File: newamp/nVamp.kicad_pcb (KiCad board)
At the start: 2 copper layers, 8 parts, among them J1 CONN_01X02, J2 CONN_01X02, U1 TS912

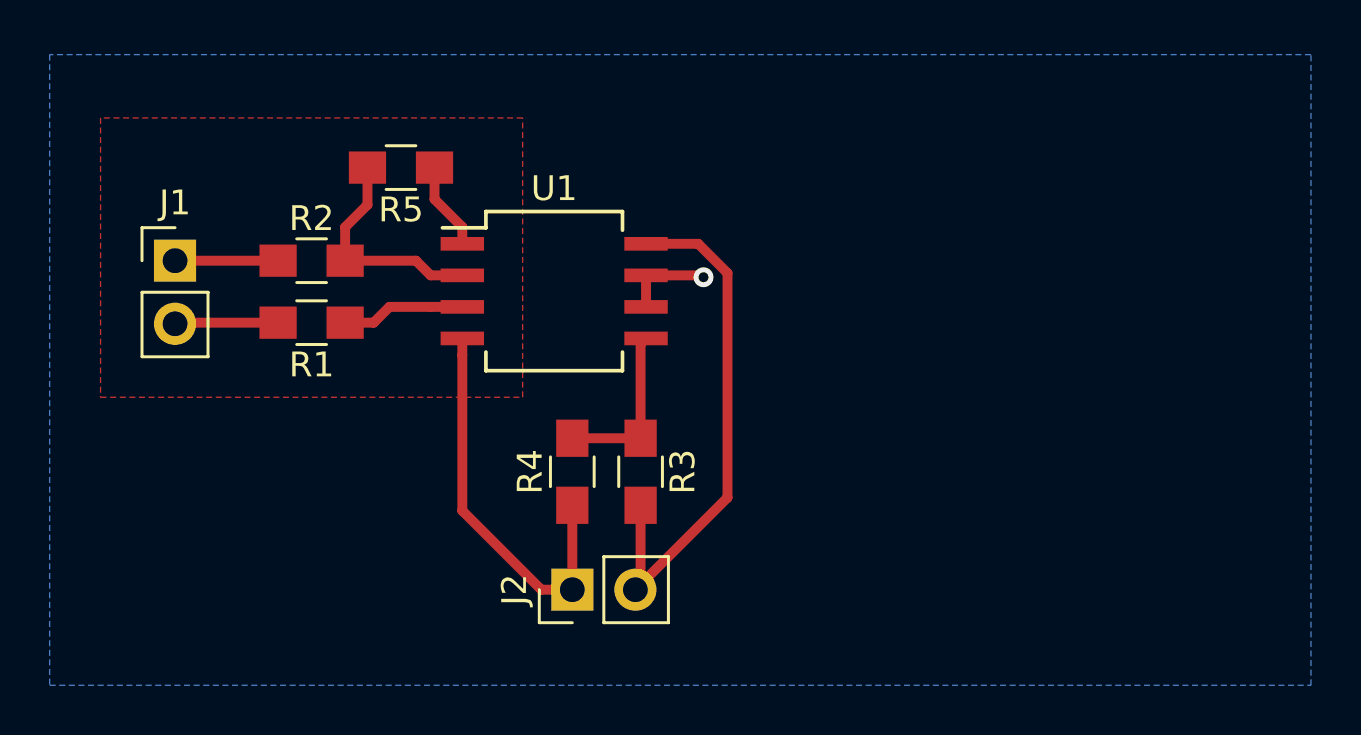
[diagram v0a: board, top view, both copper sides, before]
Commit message: Update PCB to use AD8428 and AD4528 amps
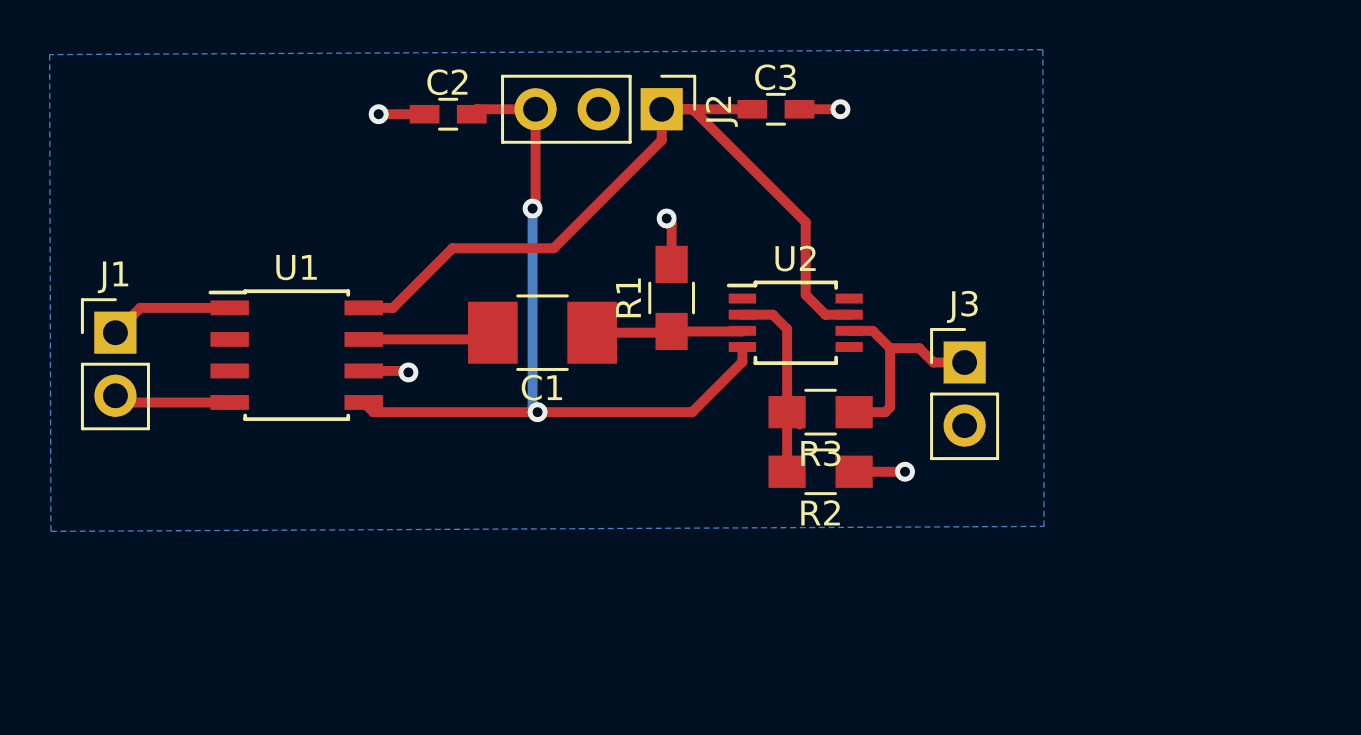
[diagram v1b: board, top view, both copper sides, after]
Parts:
- removed R4: 1k, Resistors_SMD:R_0805_HandSoldering
- removed R5: 10k, Resistors_SMD:R_0805_HandSoldering
- added C1: 100u, Capacitors_SMD:C_1210_HandSoldering, F.Cu at (127.8, 87.4)
- added C2: 100n, Capacitors_SMD:C_0603_HandSoldering, F.Cu at (124.0, 78.6)
- added C3: 100n, Capacitors_SMD:C_0603_HandSoldering, F.Cu at (137.2, 78.4)
- added J3: CONN_01X02, Pin_Headers:Pin_Header_Straight_1x02_Pitch2.54mm, F.Cu at (144.8, 88.6)
- added U2: ADA4528, Housings_SSOP:TSSOP-8_3x3mm_Pitch0.65mm, F.Cu at (138.0, 87.0)
- J2: value CONN_01X02 -> CONN_01X03; footprint Pin_Headers:Pin_Header_Straight_1x02_Pitch2.54mm -> Pin_Headers:Pin_Header_Straight_1x03_Pitch2.54mm
- R1: value 0 -> 15k
- R3: value 1k -> 100k
- U1: value TS912 -> AD8428; footprint Housings_SOIC:SO-8_5.3x6.2mm_Pitch1.27mm -> Housings_SOIC:SOIC-8_3.9x4.9mm_Pitch1.27mm
- moved R2 22.2 mm to (139.0, 93.0), turned to 180 degrees
- moved J2 19.7 mm to (132.6, 78.4), turned to 270 degrees
- moved R1 14.5 mm to (133.0, 86.0), turned to 90 degrees
- moved U1 10.7 mm to (117.9, 88.3)
- moved R3 7.64 mm to (139.0, 90.6), turned to 180 degrees
- moved J1 3.76 mm to (110.6, 87.4)
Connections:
- J2 pad 1: GNDPWR -> VDD
- J2 pad 2: +3V3 -> GND
- R1 pad 1: Net-(R1-Pad1) -> Net-(C1-Pad1)
- R1 pad 2: Net-(J1-Pad2) -> GND
- R2 pad 2: /FB -> Net-(R2-Pad2)
- R3 pad 1: Net-(R3-Pad1) -> Net-(J3-Pad1)
- R3 pad 2: +3V3 -> Net-(R2-Pad2)
- U1 pad 1: Net-(R5-Pad1) -> GND
- U1 pad 2: /FB -> Net-(U1-Pad2)
- U1 pad 3: Net-(R1-Pad1) -> Net-(U1-Pad3)
- U1 pad 4: GNDPWR -> Net-(J1-Pad2)
- U1 pad 5: Net-(R3-Pad1) -> VEE
- U1 pad 7: GND -> Net-(C1-Pad2)
- U1 pad 8: +3V3 -> VDD
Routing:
- net VDD: track 0.00 -> 32.4 mm
- net VEE: track 0.00 -> 31.8 mm, vias 0 -> 2
- net +3V3: track 21.5 -> 0.00 mm
- net GNDPWR: track 16.1 -> 0.00 mm
- net /FB: track 9.09 -> 0.00 mm
- net Net-(J3-Pad1): track 0.00 -> 9.09 mm
- net Net-(R2-Pad2): track 0.00 -> 8.50 mm
- net Net-(R3-Pad1): track 6.61 -> 0.00 mm
- net GND: track 7.77 -> 14.3 mm, vias 1 -> 5
- net Net-(C1-Pad1): track 0.00 -> 6.08 mm
- net Net-(C1-Pad2): track 0.00 -> 5.31 mm
- net Net-(R1-Pad1): track 4.98 -> 0.00 mm
- net Net-(R5-Pad1): track 3.53 -> 0.00 mm
- net Net-(J1-Pad2): track 4.17 -> 4.71 mm
- removed copper zone on F.Cu, net /FB

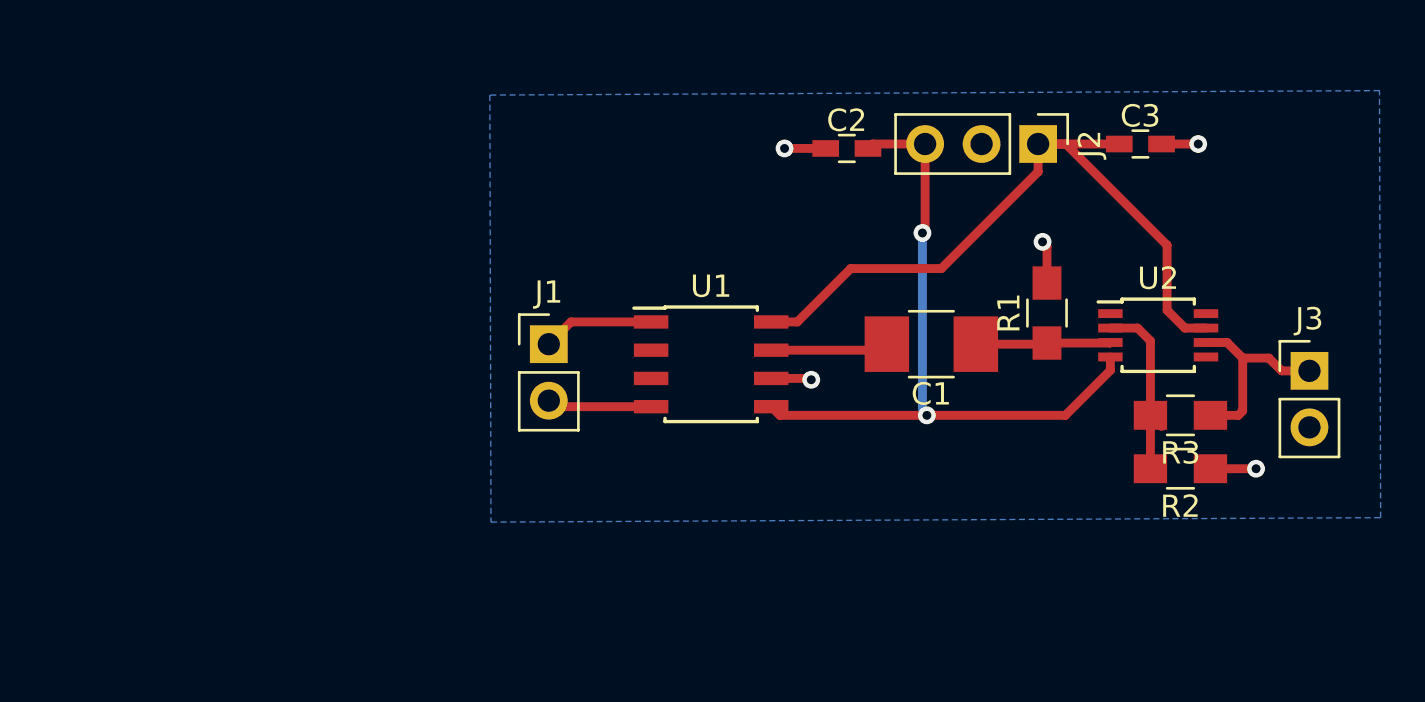
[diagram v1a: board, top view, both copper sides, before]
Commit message: Update PCB to use two AD8428s for lower noise
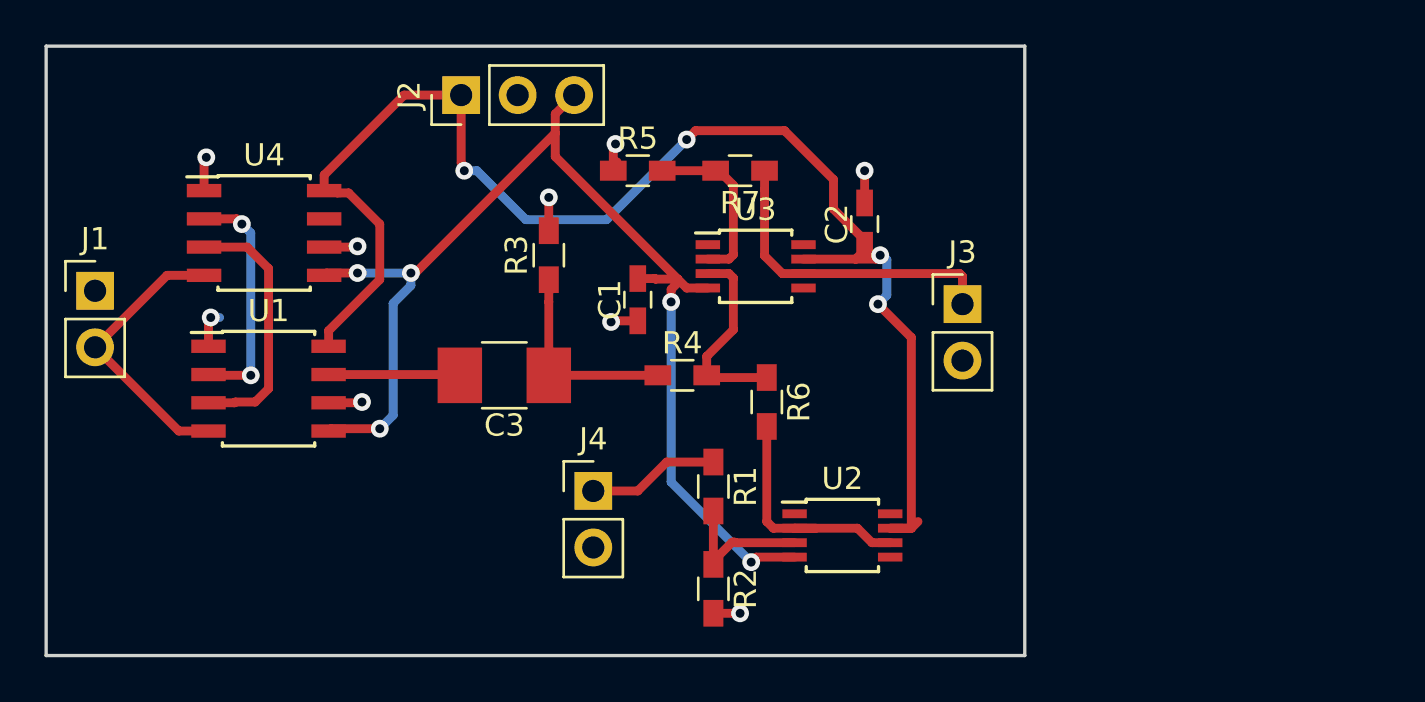
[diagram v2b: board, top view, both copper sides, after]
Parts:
- added J4: CONN_01X02, Pin_Headers:Pin_Header_Straight_1x02_Pitch2.54mm, F.Cu at (112.6, 94.0)
- added R4: 100, Resistors_SMD:R_0603_HandSoldering, F.Cu at (116.6, 88.8)
- added R5: 100, Resistors_SMD:R_0603_HandSoldering, F.Cu at (114.6, 79.6)
- added R6: 33k, Resistors_SMD:R_0603_HandSoldering, F.Cu at (120.4, 90.0)
- added R7: 33k, Resistors_SMD:R_0603_HandSoldering, F.Cu at (119.2, 79.6)
- added U3: ADA4528, Housings_SSOP:TSSOP-8_3x3mm_Pitch0.65mm, F.Cu at (119.9, 83.9)
- added U4: AD8428, Housings_SOIC:SOIC-8_3.9x4.9mm_Pitch1.27mm, F.Cu at (97.8, 82.4)
- C1: value 100u -> 100n; footprint Capacitors_SMD:C_1210_HandSoldering -> Capacitors_SMD:C_0603_HandSoldering
- C3: value 100n -> 100u; footprint Capacitors_SMD:C_0603_HandSoldering -> Capacitors_SMD:C_1210_HandSoldering
- R1: value 15k -> 1k; footprint Resistors_SMD:R_0805_HandSoldering -> Resistors_SMD:R_0603_HandSoldering
- R2: value 100 -> 1k; footprint Resistors_SMD:R_0805_HandSoldering -> Resistors_SMD:R_0603_HandSoldering
- R3: value 100k -> 15k; footprint Resistors_SMD:R_0805_HandSoldering -> Resistors_SMD:R_0603_HandSoldering
- moved C3 30.4 mm to (108.6, 88.8), turned to 180 degrees
- moved R3 29.3 mm to (110.6, 83.4), turned to 90 degrees
- moved J2 26.0 mm to (106.7, 76.2), turned to 90 degrees
- moved R2 21.7 mm to (118.0, 98.4), turned to 270 degrees
- moved J1 20.5 mm to (90.2, 85.0)
- moved U1 19.9 mm to (98.0, 89.4)
- moved R1 16.9 mm to (118.0, 93.8), turned to 270 degrees
- moved U2 16.8 mm to (123.8, 96.0)
- moved J3 15.9 mm to (129.2, 85.6)
- moved C1 13.4 mm to (114.6, 85.4), turned to 90 degrees
- moved C2 3.49 mm to (124.8, 82.0), turned to 90 degrees
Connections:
- net Net-(J1-Pad2) renamed /IN+
- C1 pad 1: Net-(C1-Pad1) -> GND
- C1 pad 2: Net-(C1-Pad2) -> VEE
- C2 pad 1: GND -> VDD
- C2 pad 2: VEE -> GND
- C3 pad 1: VDD -> Net-(C3-Pad1)
- C3 pad 2: GND -> Net-(C3-Pad2)
- R1 pad 1: Net-(C1-Pad1) -> +3V3
- R1 pad 2: GND -> Net-(R1-Pad2)
- R2 pad 1: GND -> Net-(R1-Pad2)
- R2 pad 2: Net-(R2-Pad2) -> GND
- R3 pad 1: Net-(J3-Pad1) -> Net-(C3-Pad1)
- R3 pad 2: Net-(R2-Pad2) -> GND
- U1 pad 2: Net-(U1-Pad2) -> /Filt+
- U1 pad 3: Net-(U1-Pad3) -> /Filt-
- U1 pad 7: Net-(C1-Pad2) -> Net-(C3-Pad2)
- U2 pad 2: Net-(R2-Pad2) -> /VRef
- U2 pad 3: Net-(C1-Pad1) -> Net-(R1-Pad2)
- U2 pad 6: Net-(J3-Pad1) -> /VRef
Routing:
- net VDD: track 32.4 -> 64.9 mm, vias 0 -> 4
- net VEE: track 31.8 -> 53.6 mm, vias 2 -> 5
- net /Filt-: track 0.00 -> 12.6 mm
- net /VRef: track 0.00 -> 11.2 mm
- net /Filt+: track 0.00 -> 10.7 mm, vias 0 -> 2
- net Net-(C3-Pad1): track 0.00 -> 9.20 mm
- net Net-(R4-Pad2): track 0.00 -> 8.85 mm
- net Net-(R2-Pad2): track 8.50 -> 0.00 mm
- net /IN+: track 4.71 -> 12.9 mm
- net Net-(R5-Pad2): track 0.00 -> 7.83 mm
- net Net-(R1-Pad2): track 0.00 -> 6.56 mm
- net Net-(C1-Pad1): track 6.08 -> 0.00 mm
- net +3V3: track 0.00 -> 5.94 mm
- net Net-(C3-Pad2): track 0.00 -> 5.91 mm
- net Net-(C1-Pad2): track 5.31 -> 0.00 mm
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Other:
- board outline added: 44 x 27.4 mm

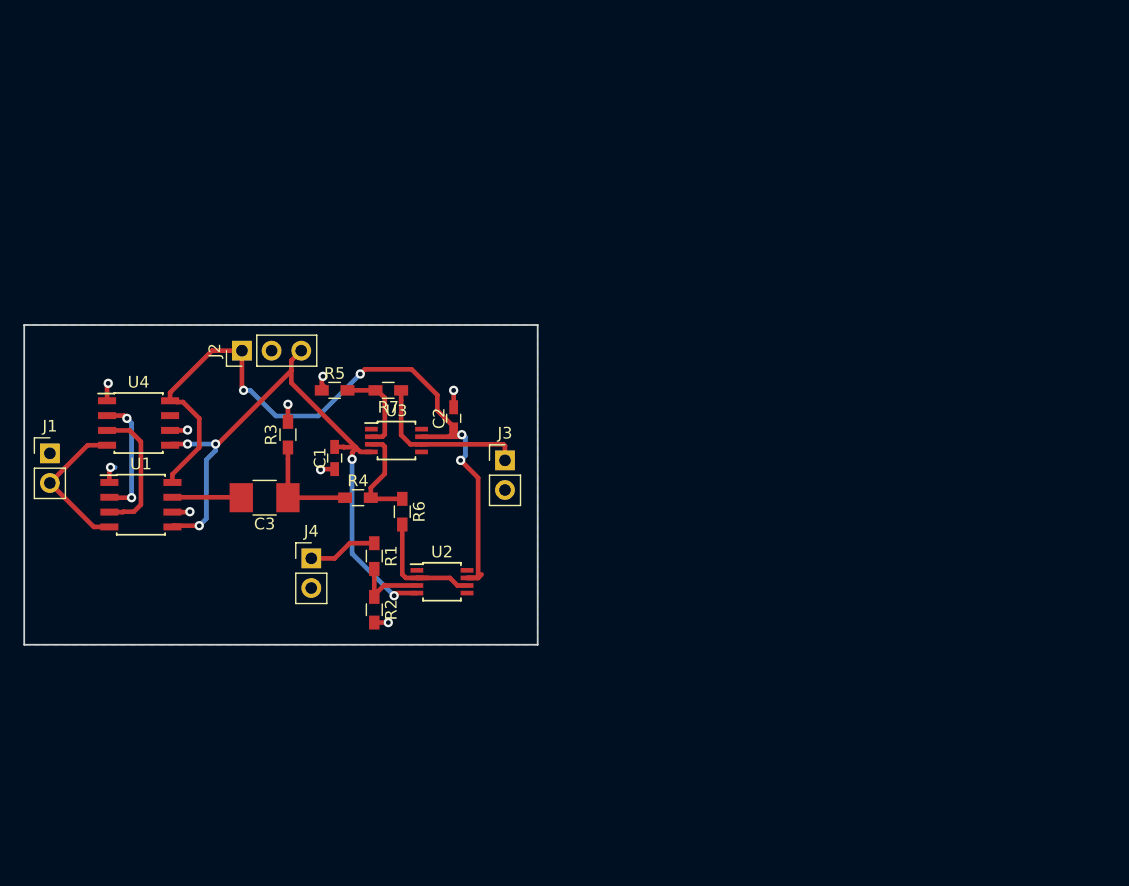
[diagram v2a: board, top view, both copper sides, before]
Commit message: Make a better, 4 layer design for nVamp
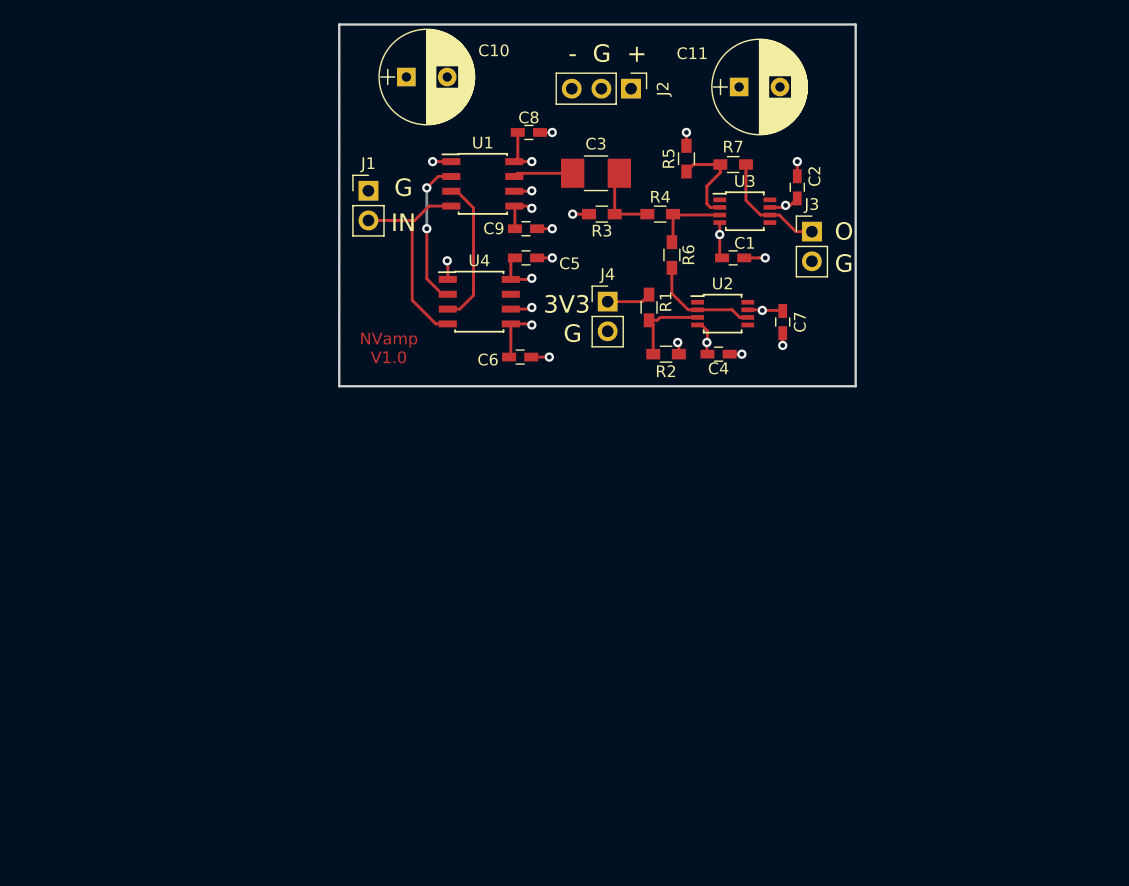
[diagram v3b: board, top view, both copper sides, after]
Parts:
- added C10: CP, Capacitors_THT:CP_Radial_D8.0mm_P3.50mm, F.Cu at (120.8, 52.8)
- added C11: CP, Capacitors_THT:CP_Radial_D8.0mm_P3.50mm, F.Cu at (149.3, 53.6)
- added C4: 100n, Capacitors_SMD:C_0603_HandSoldering, F.Cu at (147.5, 76.5)
- added C5: 100n, Capacitors_SMD:C_0603_HandSoldering, F.Cu at (131.0, 65.8)
- added C6: 100n, Capacitors_SMD:C_0603_HandSoldering, F.Cu at (130.5, 76.8)
- added C7: 100n, Capacitors_SMD:C_0603_HandSoldering, F.Cu at (153.0, 73.8)
- added C8: 100n, Capacitors_SMD:C_0603_HandSoldering, F.Cu at (131.2, 57.5)
- added C9: 100n, Capacitors_SMD:C_0603_HandSoldering, F.Cu at (131.0, 68.2)
- moved J2 40.2 mm to (140.0, 53.8), turned to 270 degrees
- moved U1 40.2 mm to (127.3, 61.9)
- moved C3 39.7 mm to (137.0, 61.0)
- moved C1 38.2 mm to (148.8, 68.2), turned to 180 degrees
- moved R5 36.1 mm to (144.8, 59.8), turned to 270 degrees
- moved U3 35.7 mm to (149.8, 64.2)
- moved R4 35.5 mm to (142.5, 64.5)
- moved C2 35.5 mm to (154.2, 62.2)
- moved J1 35.4 mm to (117.5, 62.5)
- moved R7 35.3 mm to (148.8, 60.2)
- moved J4 33.6 mm to (138.0, 72.0)
- moved U2 33.3 mm to (147.8, 73.0)
- moved R2 33.2 mm to (143.0, 76.5), turned to 0 degrees
- moved R3 32.9 mm to (137.5, 64.5), turned to 180 degrees
- moved J3 32.8 mm to (155.5, 66.0)
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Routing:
- net VDD: track 64.9 -> 13.9 mm
- net VEE: track 53.6 -> 14.5 mm, vias 5 -> 4
- net GND: track 13.3 -> 20.5 mm, vias 9 -> 15
- net /IN+: track 12.9 -> 18.3 mm
- net Net-(J3-Pad1): track 14.4 -> 9.83 mm
- net Net-(C3-Pad1): track 9.20 -> 6.47 mm
- net Net-(R4-Pad2): track 8.85 -> 6.47 mm
- net +3V3: track 5.94 -> 3.79 mm
- net /Filt+: track 10.7 -> 12.6 mm
- net /VRef: track 11.2 -> 9.70 mm
- net Net-(C3-Pad2): track 5.91 -> 5.11 mm
- net Net-(R1-Pad2): track 6.56 -> 7.31 mm
- added copper zone on In1.Cu, net GND
- added copper zone on In2.Cu, net VDD
- added copper zone on B.Cu, net VEE
- removed copper zone on B.Cu, net GND
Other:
- board size 44 x 27.4 mm -> 44.2 x 31 mm
- copper layers 2 -> 4
- net class Default: trace_width 0.4 -> 0.25
- rule pad_to_mask_clearance: 0.2 -> 0
- board text added: "+"
- board text added: "-"
- board text added: "3V3"
- board text added: "G"
- board text added: "IN"
- board text added: "NVamp V1.0"
- board text added: "O"
